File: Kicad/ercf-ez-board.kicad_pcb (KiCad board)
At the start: 2 copper layers, 90.8 x 35.6 mm, 27 parts, among them J1 Conn_01x03_Male, J2 Conn_01x03_Male, J3 Conn_01x03_Male, J4 Conn_01x03_Male, J5 Screw_Terminal_01x02, J6 Conn_01x05_Male, J7 Conn_01x04_Male, J8 Conn_01x04_Male, U1 SeeeduinoXIAO, U2 L7805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

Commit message: Open 2nd jumper
Open the jumper for the second UART pin
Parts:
- JP7, JP9: footprint Jumper:SolderJumper-2_P1.3mm_Bridged_RoundedPad1.0x1.5mm -> Jumper:SolderJumper-2_P1.3mm_Open_RoundedPad1.0x1.5mm

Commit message: Fix accidently remove the logo
Fix accidentally remove the logo
Minor typo in readme
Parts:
- added G***: LOGO, ercf-ez-board:ercf-logo-mini, F.Cu at (133.2, 139.0)

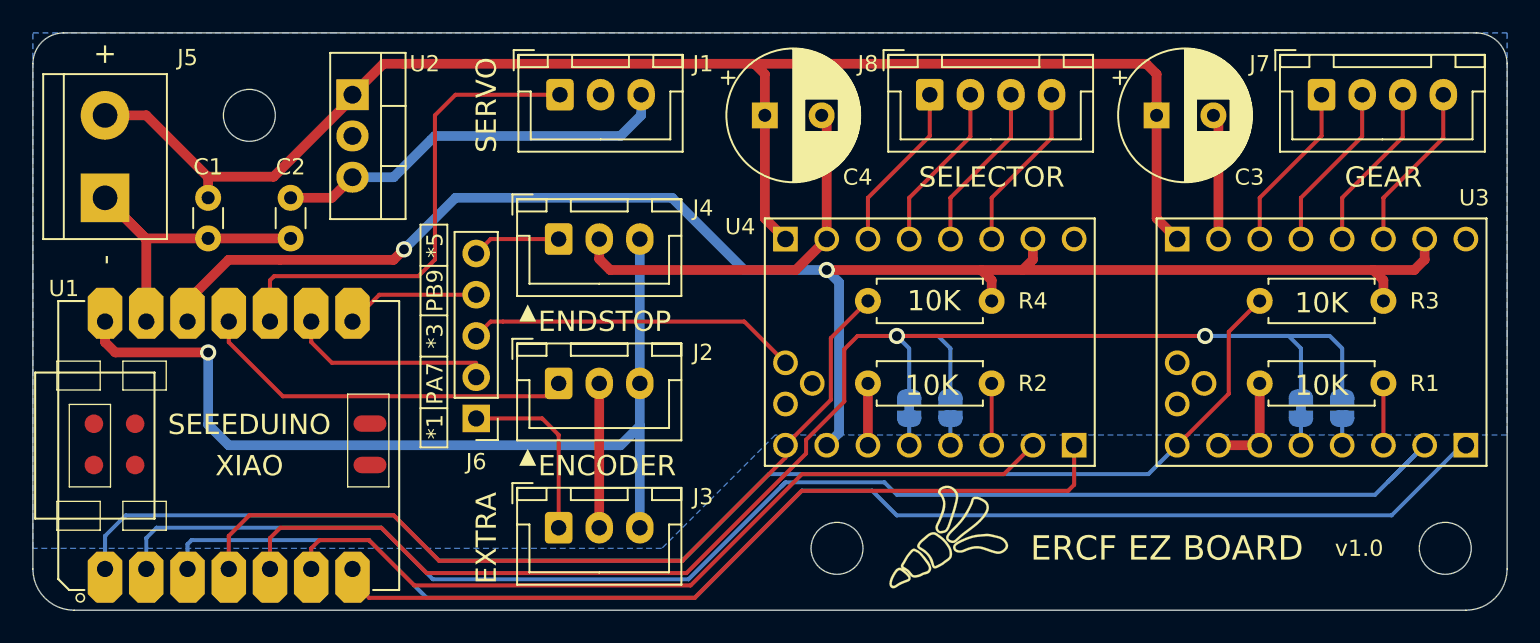
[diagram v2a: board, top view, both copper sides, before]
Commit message: PCB v1.1
PCB v1.1:
- VCC for endstop, encoder and extra are now 3V3
- Fix gear stepper ground plane was not connected to GND
- Improve the tracks width for power and motors
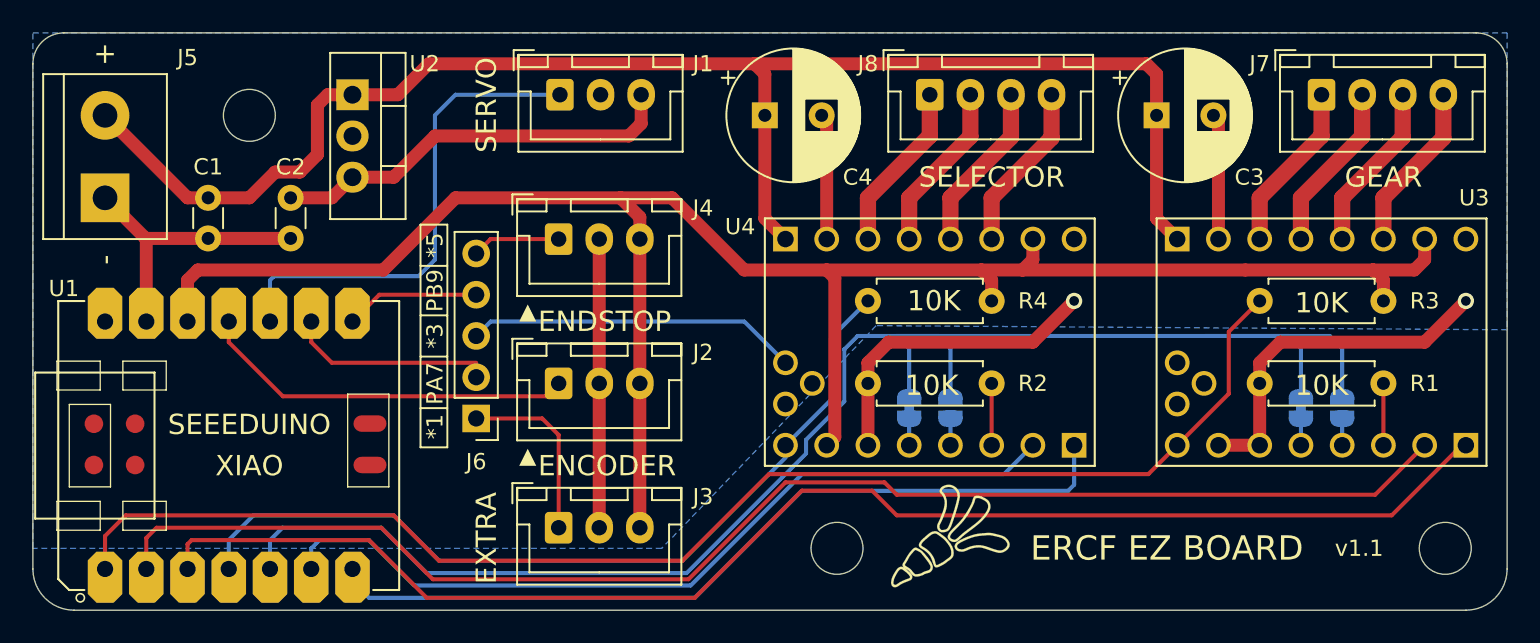
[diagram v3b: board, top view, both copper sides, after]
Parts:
- removed the JP10 at (130.8, 131.1)
- removed the JP8 at (154.9, 131.1)
- added JP7: Jumper_NO_Small, Jumper:SolderJumper-2_P1.3mm_Open_RoundedPad1.0x1.5mm, B.Cu at (157.5, 131.1)
- added JP9: Jumper_NO_Small, Jumper:SolderJumper-2_P1.3mm_Open_RoundedPad1.0x1.5mm, B.Cu at (133.3, 131.1)
- JP10: renamed from JP9; footprint Jumper:SolderJumper-2_P1.3mm_Open_RoundedPad1.0x1.5mm -> Jumper:SolderJumper-2_P1.3mm_Bridged_RoundedPad1.0x1.5mm
- JP8: renamed from JP7; footprint Jumper:SolderJumper-2_P1.3mm_Open_RoundedPad1.0x1.5mm -> Jumper:SolderJumper-2_P1.3mm_Bridged_RoundedPad1.0x1.5mm
- moved JP10 2.54 mm to (130.8, 131.1)
- moved JP8 2.54 mm to (154.9, 131.1)
- moved G*** 0.12 mm to (133.3, 138.9)
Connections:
- J2 pad 3: VCC -> +3V3
- J3 pad 3: VCC -> +3V3
- J4 pad 3: VCC -> +3V3
- JP10 pad 2: Net-(JP9-Pad2) -> Net-(JP10-Pad2)
- JP8 pad 2: Net-(JP7-Pad2) -> Net-(JP8-Pad2)
- U1 pad 14: VCC -> (no net)
- U3 pad JP1_4: Net-(JP7-Pad2) -> Net-(JP7-Pad1)
- U4 pad JP1_4: Net-(JP9-Pad2) -> Net-(JP9-Pad1)
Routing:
- net VCC: track 57.7 -> 0.00 mm, vias 1 -> 0
- net +3V3: track 101.4 -> 124.3 mm, vias 2 -> 0
- net GND: track 72.0 -> 92.1 mm, vias 0 -> 2
- net G-STEP: track 92.7 -> 86.3 mm
- net VDC: track 93.2 -> 94.8 mm
- net Net-(JP9-Pad2): track 1.64 -> 0.00 mm
- net Net-(JP9-Pad1): track 0.00 -> 1.64 mm
- net Net-(JP7-Pad2): track 1.64 -> 0.00 mm
- net Net-(JP7-Pad1): track 0.00 -> 1.64 mm
- net UART: track 101.2 -> 101.1 mm, vias 2 -> 0
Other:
- net class MOT added: clearance 0.2, trace_width 1, via_dia 1, via_drill 0.6
- net class POWER removed
- net class PWR added: clearance 0.2, trace_width 0.8, via_dia 1, via_drill 0.6
- board text added: "ERCF EZ BOARD v1.1"
- board text added: "v1.1"
- board text removed: "ERCF EZ BOARD v1.0"
- board text removed: "v1.0"
